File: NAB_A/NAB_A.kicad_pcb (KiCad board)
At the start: 2 copper layers, 35 x 30 mm, 44 parts, among them K1 кнопка, K2 кнопка, X1 Check_point

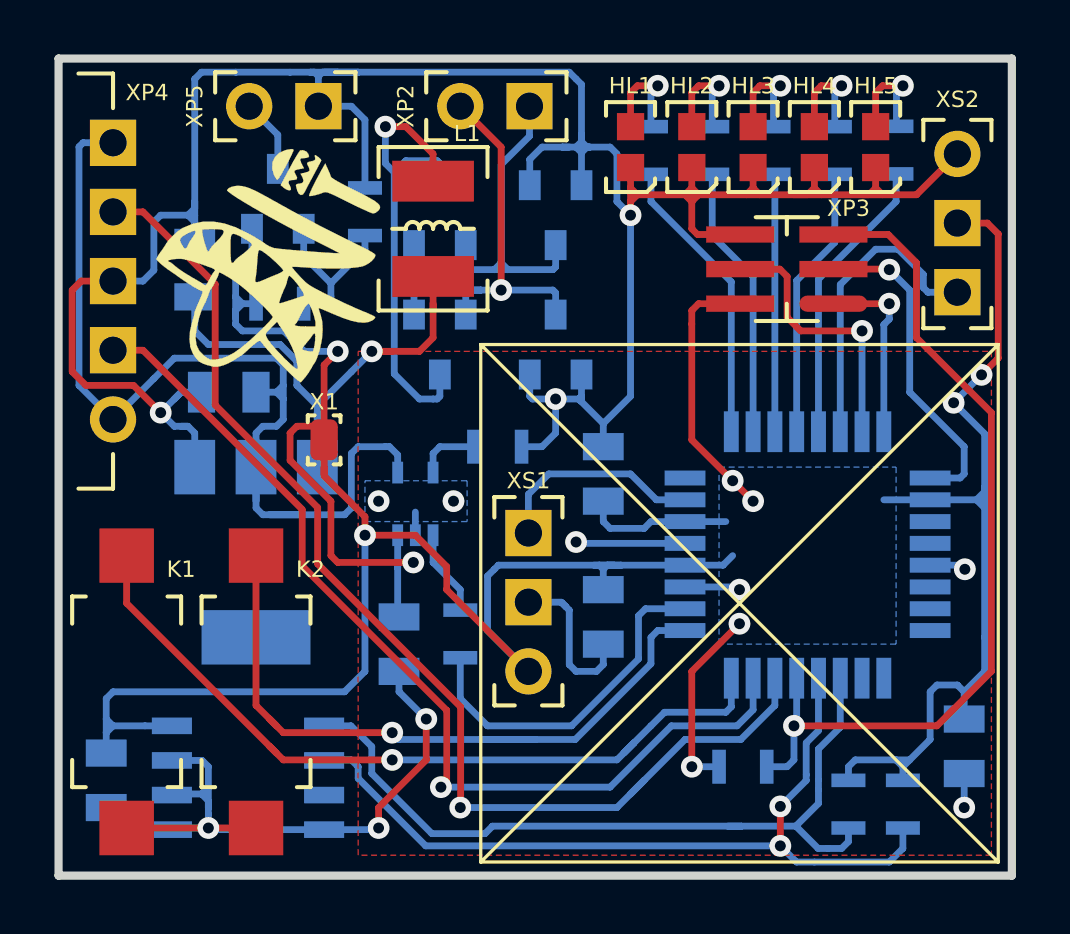
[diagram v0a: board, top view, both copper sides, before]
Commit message: NAB_A: 433data перенесен на uart-tx, заведена аналоговая часть, +silk
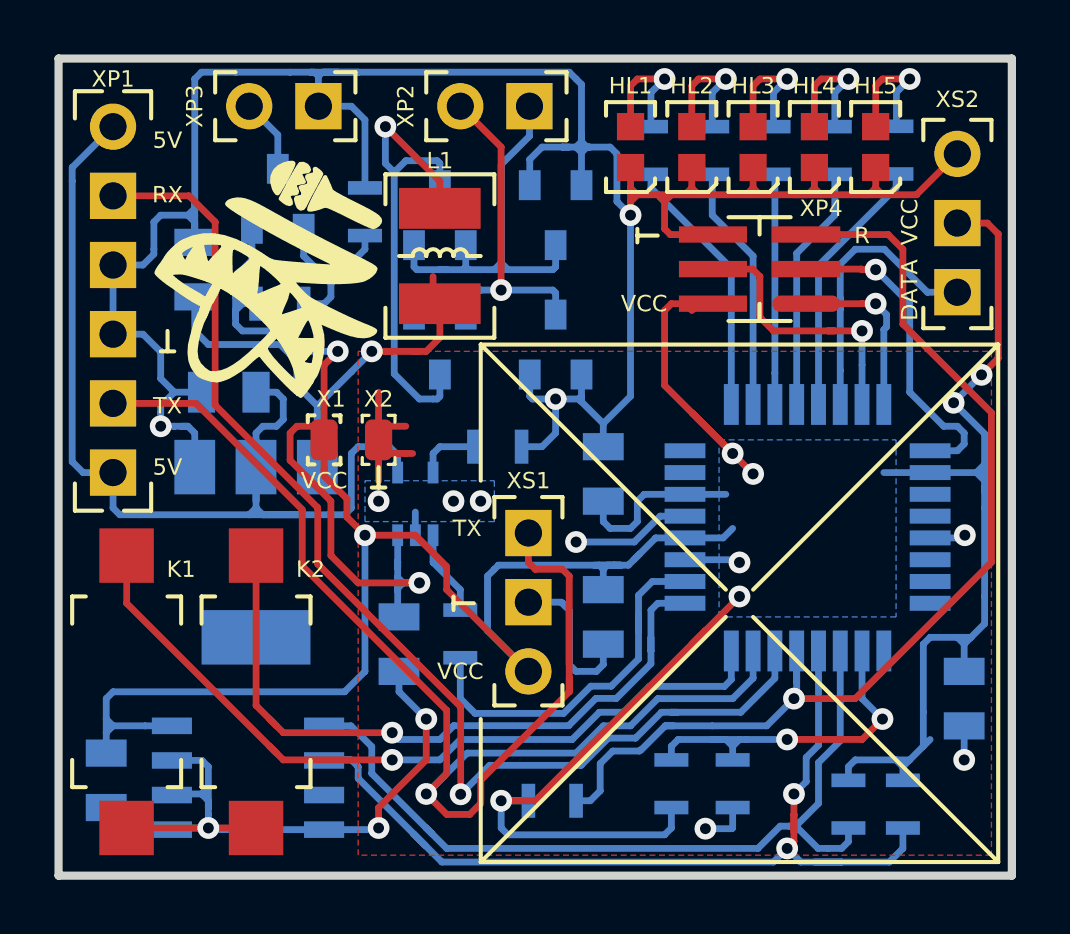
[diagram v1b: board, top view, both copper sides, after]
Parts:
- removed the XP4 at (212.0, 43.1)
- added R3: Резистор_0,065Вт, N_RLC:Резистор_SMD_0603_0,065_Вт, B.Cu at (232.5, 67.5)
- added R4: Резистор_0,065Вт, N_RLC:Резистор_SMD_0603_0,065_Вт, B.Cu at (234.8, 65.8)
- added X2: Check_point, N_X:Пробник, F.Cu at (221.8, 54.0)
- added XP1: Вилка_PLS6, N_X:Вилка_PLS6_вертикальная, F.Cu at (212.0, 42.5)
- moved R5 7.11 mm to (229.0, 67.2)
- moved C5 1.75 mm to (243.2, 62.5)
- moved L1 1.03 mm to (224.0, 45.5)
- moved DD1 1.00 mm to (233.2, 60.0)
- moved XP4 1.00 mm to (236.5, 49.0)
- moved LOGO1 0.50 mm to (218.2, 47.5)
- renumbered C3 to C1, C1 to C2, C5 to C3, C2 to C4, C6 to C5, C4 to C6, DD2 to G2, R13 to R1, R2 to R10, R3 to R11, R4 to R12, R5 to R13, R11 to R14, R14 to R2, R9 to R5, R10 to R7, R12 to R8, R1 to R9, VT2 to VT1, XP5 to XP3, XP3 to XP4
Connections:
- net /BUT-1 renamed /BUTT-1
- net /BUT-2 renamed /BUTT-2
- DD1 pad 26: Net-(DD1-Pad26) -> /VBAT_MEASUR
- DD1 pad 7: /TX_DATA -> Net-(DD1-Pad7)
- XS1 pad 3: /TX_DATA -> /MC_TX
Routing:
- net /MC_VCC: track 103.9 -> 123.8 mm
- net /MC_TX: track 35.6 -> 51.9 mm
- net /VBAT_MEASUR: track 0.00 -> 13.2 mm, vias 0 -> 2
- net /TX_DATA: track 7.87 -> 0.00 mm
- net /nRESET: track 32.8 -> 40.3 mm
- net /GND: track 147.6 -> 151.9 mm, vias 12 -> 14
- net /SCL: track 30.7 -> 34.6 mm
- net /5V: track 37.3 -> 38.6 mm
- net /SDA: track 29.1 -> 30.4 mm
- net /V_BAT: track 25.7 -> 26.9 mm
- net /CHARGE_STATUS: track 12.9 -> 13.9 mm
- net /HL-5: track 10.6 -> 9.63 mm
- net /HL-4: track 10.0 -> 9.03 mm
- net /HL-2: track 10.1 -> 9.07 mm
- net /HL-1: track 10.7 -> 9.67 mm
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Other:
- board text added: "5V"
- board text added: "DATA"
- board text added: "R"
- board text added: "RX"
- board text added: "TX"
- board text added: "VCC"

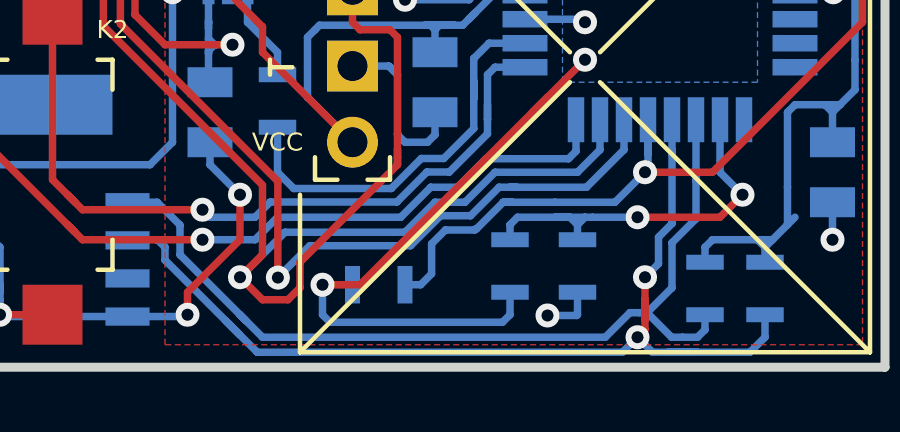
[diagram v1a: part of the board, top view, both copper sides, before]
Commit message: NAB_A: добавлен ID на плату, подготовлены GERBER
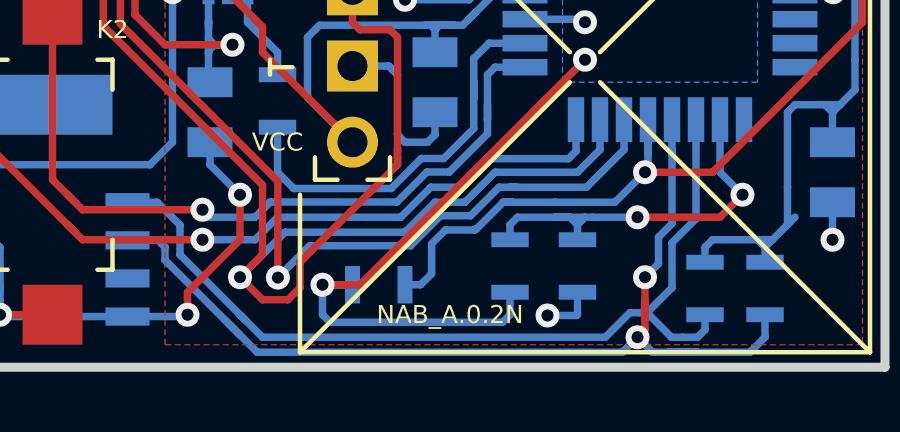
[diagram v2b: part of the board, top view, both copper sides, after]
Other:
- board text added: "NAB_A.0.2N"
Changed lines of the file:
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@@
-(kicad_pcb (version 20171130) (host pcbnew "(5.1.2-1)-1")
+(kicad_pcb (version 20171130) (host pcbnew "(5.1.4)-1")
   (general
     (thickness 1.6)
-    (drawings 34)
+    (drawings 35)
     (tracks 709)
     (zones 0)
@@
     (solder_mask_min_width 0.25)
     (aux_axis_origin 0 0)
-    (visible_elements FFFFFF7F)
+    (visible_elements 7FFFFFFF)
     (pcbplotparams
-      (layerselection 0x010fc_ffffffff)
+      (layerselection 0x010f0_ffffffff)
       (usegerberextensions false)
       (usegerberattributes false)
@@
       (outputformat 1)
       (mirror false)
-      (drillshape 1)
+      (drillshape 0)
       (scaleselection 1)
-      (outputdirectory ""))
+      (outputdirectory "GERBER/"))
   )
   (net 0 "")
@@
     )
   )
+  (gr_text NAB_A.0.2N (at 230.5 68.25) (layer F.SilkS)
+    (effects (font (size 0.6 0.6) (thickness 0.15)))
+  )
   (gr_text DATA (at 241.25 48.5 90) (layer F.SilkS)
     (effects (font (size 0.6 0.6) (thickness 0.15)))
@@
   (gr_line (start 244.5 50.5) (end 244.5 69.5) (layer F.SilkS) (width 0.15))
   (gr_line (start 225.5 50.5) (end 244.5 50.5) (layer F.SilkS) (width 0.15))
-  (segment (start 223.75 55.2) (end 223.75 55) (width 0.25) (layer B.Cu) (net 42))
-  (segment (start 223.75 55) (end 223.75 54.5) (width 0.25) (layer B.Cu) (net 42))
-  (segment (start 223.75 54.5) (end 224 54.25) (width 0.25) (layer B.Cu) (net 42))
-  (segment (start 224 54.25) (end 225.25 54.25) (width 0.25) (layer B.Cu) (net 42))
-  (segment (start 223.75 57.5) (end 223.75 58.5) (width 0.25) (layer B.Cu) (net 43))
-  (segment (start 223.75 58.5) (end 224.75 59.5) (width 0.25) (layer B.Cu) (net 43))
-  (segment (start 224.75 59.5) (end 224.75 60.25) (width 0.25) (layer B.Cu) (net 43))
   (via (at 223.5 67) (size 0.8) (drill 0.4) (layers F.Cu B.Cu) (net 6))
   (segment (start 224.25 66.25) (end 223.5 67) (width 0.25) (layer F.Cu) (net 6))
@@
   (segment (start 234.7 47.7) (end 231.75 44.75) (width 0.25) (layer B.Cu) (net 26))
   (segment (start 234.7 52.7) (end 234.7 47.7) (width 0.25) (layer B.Cu) (net 26))
-  (segment (start 212.5 60) (end 212.5 58.25) (width 0.25) (layer F.Cu) (net 39))
-  (via (at 222.25 65.75) (size 0.8) (drill 0.4) (layers F.Cu B.Cu) (net 39))
-  (segment (start 218.25 65.75) (end 217.75 65.25) (width 0.25) (layer F.Cu) (net 39))
-  (segment (start 222.25 65.75) (end 218.25 65.75) (width 0.25) (layer F.Cu) (net 39))
-  (segment (start 217.75 65.25) (end 212.5 60) (width 0.25) (layer F.Cu) (net 39))
-  (segment (start 217.987347 65.487347) (end 217.75 65.25) (width 0.25) (layer F.Cu) (net 39))
-  (segment (start 217.25 63.75) (end 217.25 58.25) (width 0.25) (layer F.Cu) (net 40))
-  (via (at 222.25 64.75) (size 0.8) (drill 0.4) (layers F.Cu B.Cu) (net 40))
-  (segment (start 218.25 64.75) (end 217.75 64.25) (width 0.25) (layer F.Cu) (net 40))
-  (segment (start 222.25 64.75) (end 218.25 64.75) (width 0.25) (layer F.Cu) (net 40))
-  (segment (start 217.75 64.25) (end 217.25 63.75) (width 0.25) (layer F.Cu) (net 40))
-  (segment (start 218 64.5) (end 217.75 64.25) (width 0.25) (layer F.Cu) (net 40))
   (segment (start 234 45.75) (end 234 44.25) (width 0.25) (layer B.Cu) (net 27))
   (segment (start 235.5 47.25) (end 234 45.75) (width 0.25) (layer B.Cu) (net 27))
@@
   (segment (start 241.9 48.58) (end 240.32 47) (width 0.25) (layer B.Cu) (net 31))
   (segment (start 243 48.58) (end 241.9 48.58) (width 0.25) (layer B.Cu) (net 31))
-  (segment (start 219 46.25) (end 219 46) (width 0.25) (layer B.Cu) (net 44))
-  (segment (start 219 47.25) (end 219 46.25) (width 0.25) (layer B.Cu) (net 44))
-  (segment (start 220 48.25) (end 219 47.25) (width 0.25) (layer B.Cu) (net 44))
-  (segment (start 220 48.75) (end 220 48.25) (width 0.25) (layer B.Cu) (net 44))
-  (segment (start 219.75 49) (end 220 48.75) (width 0.25) (layer B.Cu) (net 44))
-  (segment (start 219 49) (end 219.75 49) (width 0.25) (layer B.Cu) (net 44))
-  (segment (start 221.25 47) (end 220 48.25) (width 0.25) (layer B.Cu) (net 44))
-  (segment (start 221.25 46.5) (end 221.25 47) (width 0.25) (layer B.Cu) (net 44))
   (segment (start 223.05 48.6) (end 223.05 49.4) (width 0.25) (layer B.Cu) (net 32))
   (segment (start 223.15 48.5) (end 223.05 48.6) (width 0.25) (layer B.Cu) (net 32))
@@
   (segment (start 239.5 63.5) (end 240.25 64.25) (width 0.25) (layer B.Cu) (net 38))
   (segment (start 239.5 61.75) (end 239.5 63.5) (width 0.25) (layer B.Cu) (net 38))
+  (segment (start 212.5 60) (end 212.5 58.25) (width 0.25) (layer F.Cu) (net 39))
+  (via (at 222.25 65.75) (size 0.8) (drill 0.4) (layers F.Cu B.Cu) (net 39))
+  (segment (start 218.25 65.75) (end 217.75 65.25) (width 0.25) (layer F.Cu) (net 39))
+  (segment (start 222.25 65.75) (end 218.25 65.75) (width 0.25) (layer F.Cu) (net 39))
+  (segment (start 217.75 65.25) (end 212.5 60) (width 0.25) (layer F.Cu) (net 39))
+  (segment (start 217.987347 65.487347) (end 217.75 65.25) (width 0.25) (layer F.Cu) (net 39))
   (segment (start 224 65.75) (end 222.25 65.75) (width 0.25) (layer B.Cu) (net 39))
   (segment (start 224.75 65) (end 224 65.75) (width 0.25) (layer B.Cu) (net 39))
@@
   (segment (start 234.7 62.8) (end 234.45001 63.04999) (width 0.25) (layer B.Cu) (net 39))
   (segment (start 234.7 61.75) (end 234.7 62.8) (width 0.25) (layer B.Cu) (net 39))
+  (segment (start 217.25 63.75) (end 217.25 58.25) (width 0.25) (layer F.Cu) (net 40))
+  (via (at 222.25 64.75) (size 0.8) (drill 0.4) (layers F.Cu B.Cu) (net 40))
+  (segment (start 218.25 64.75) (end 217.75 64.25) (width 0.25) (layer F.Cu) (net 40))
+  (segment (start 222.25 64.75) (end 218.25 64.75) (width 0.25) (layer F.Cu) (net 40))
+  (segment (start 217.75 64.25) (end 217.25 63.75) (width 0.25) (layer F.Cu) (net 40))
+  (segment (start 218 64.5) (end 217.75 64.25) (width 0.25) (layer F.Cu) (net 40))
   (segment (start 224.507489 64.492511) (end 224 65) (width 0.25) (layer B.Cu) (net 40))
   (segment (start 228.728901 64.492511) (end 224.507489 64.492511) (width 0.25) (layer B.Cu) (net 40))
@@
   (segment (start 231.75 60.25) (end 232 60) (width 0.25) (layer B.Cu) (net 40))
   (segment (start 232 60) (end 233 60) (width 0.25) (layer B.Cu) (net 40))
+  (segment (start 223.75 55.2) (end 223.75 55) (width 0.25) (layer B.Cu) (net 42))
+  (segment (start 223.75 55) (end 223.75 54.5) (width 0.25) (layer B.Cu) (net 42))
+  (segment (start 223.75 54.5) (end 224 54.25) (width 0.25) (layer B.Cu) (net 42))
+  (segment (start 224 54.25) (end 225.25 54.25) (width 0.25) (layer B.Cu) (net 42))
+  (segment (start 223.75 57.5) (end 223.75 58.5) (width 0.25) (layer B.Cu) (net 43))
+  (segment (start 223.75 58.5) (end 224.75 59.5) (width 0.25) (layer B.Cu) (net 43))
+  (segment (start 224.75 59.5) (end 224.75 60.25) (width 0.25) (layer B.Cu) (net 43))
+  (segment (start 219 46.25) (end 219 46) (width 0.25) (layer B.Cu) (net 44))
+  (segment (start 219 47.25) (end 219 46.25) (width 0.25) (layer B.Cu) (net 44))
+  (segment (start 220 48.25) (end 219 47.25) (width 0.25) (layer B.Cu) (net 44))
+  (segment (start 220 48.75) (end 220 48.25) (width 0.25) (layer B.Cu) (net 44))
+  (segment (start 219.75 49) (end 220 48.75) (width 0.25) (layer B.Cu) (net 44))
+  (segment (start 219 49) (end 219.75 49) (width 0.25) (layer B.Cu) (net 44))
+  (segment (start 221.25 47) (end 220 48.25) (width 0.25) (layer B.Cu) (net 44))
+  (segment (start 221.25 46.5) (end 221.25 47) (width 0.25) (layer B.Cu) (net 44))
   (zone (net 18) (net_name /MC_VCC) (layer B.Cu) (hatch edge 0.508)
     (connect_pads (clearance 0.5))
